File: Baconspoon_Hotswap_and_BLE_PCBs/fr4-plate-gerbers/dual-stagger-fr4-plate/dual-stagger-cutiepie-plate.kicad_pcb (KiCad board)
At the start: 2 copper layers, 200 x 88.2 mm, 0 parts

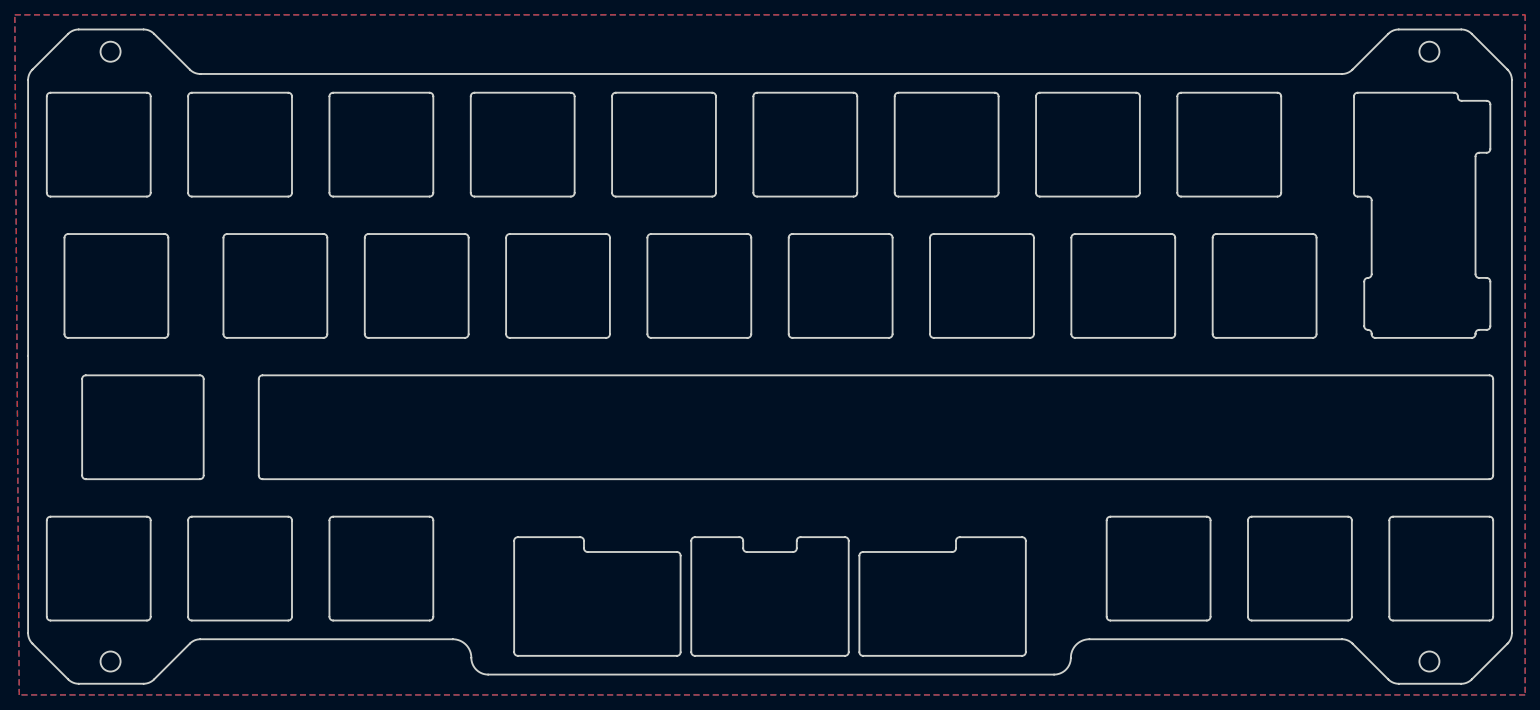
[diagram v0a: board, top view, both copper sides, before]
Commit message: Updated fabrication files for dual-stagger and ortho PCBs and plates. Added stabilizer support for dual-stagger ISO P-key. Updated readme. Updated part mumbers in BOMs and corrected position files. Added KLEs for PCB layouts.
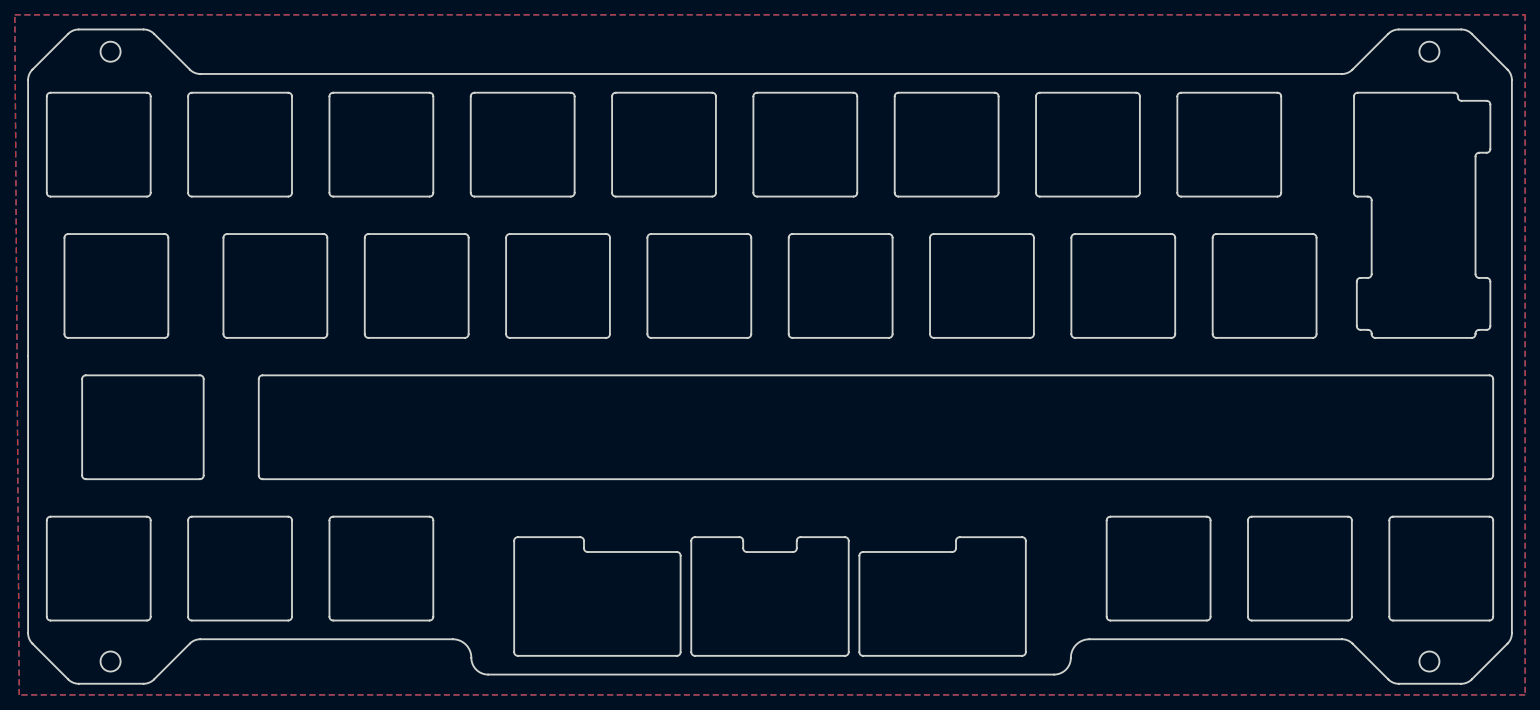
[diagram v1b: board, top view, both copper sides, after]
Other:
- outline, holes or cut-outs redrawn
- board text added: "JLCJLCJLCJLC"
